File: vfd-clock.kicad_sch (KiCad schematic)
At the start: 93 parts, among them J1 ARGB, J2 ESP-Connector, J3 I2C, J4 SWD, J5 Power Input, Q1 FDS2734, SW1 PTS815, U1 IV-17, U10 LT3757AEMSE, U11 MIC4811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

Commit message: Final workings
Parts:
- C21: footprint Capacitor_SMD:C_0603_1608Metric_Pad1.08x0.95mm_HandSolder -> Capacitor_SMD:C_0805_2012Metric_Pad1.18x1.45mm_HandSolder
- C22: footprint Resistor_SMD:R_0603_1608Metric_Pad0.98x0.95mm_HandSolder -> Capacitor_SMD:C_0603_1608Metric_Pad1.08x0.95mm_HandSolder
- C23: footprint Capacitor_SMD:C_1206_3216Metric_Pad1.33x1.80mm_HandSolder -> Capacitor_SMD:C_0805_2012Metric_Pad1.18x1.45mm_HandSolder
- D2: footprint Diode_SMD:D_SMB_Handsoldering -> Diode_SMD:D_SMF
- U14: value ~ -> SN74HCS08
- U8: value ~ -> SN74HCS541
- U9: value ~ -> HV5812
- V1, V2: footprint mynixies:mynixies-IV-1 -> mynixies:IV-1
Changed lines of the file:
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@@
 			)
 		)
-		(property "Footprint" "Capacitor_SMD:C_1206_3216Metric_Pad1.33x1.80mm_HandSolder"
+		(property "Footprint" "Capacitor_SMD:C_0805_2012Metric_Pad1.18x1.45mm_HandSolder"
 			(at 257.5052 261.62 0)
 			(effects
@@
 			)
 		)
-		(property "Value" "~"
-			(at 175.26 182.88 0)
+		(property "Value" "HV5812"
+			(at 175.26 223.52 0)
 			(effects
 				(font
@@
 			)
 		)
-		(property "Description" ""
+		(property "Description" "Unpolarized capacitor"
 			(at 91.44 191.77 0)
 			(effects
@@
 			)
 		)
-		(property "Value" "~"
-			(at 345.44 184.15 0)
+		(property "Value" "SN74HCS08"
+			(at 345.44 204.47 0)
 			(effects
 				(font
@@
 			)
 		)
-		(property "Footprint" "mynixies:mynixies-IV-1"
+		(property "Footprint" "mynixies:IV-1"
 			(at 401.32 130.81 0)
 			(effects
@@
 			)
 		)
-		(property "Description" ""
+		(property "Description" "Unpolarized capacitor"
 			(at 45.72 203.2 0)
 			(effects
@@
 			)
 		)
-		(property "Description" ""
+		(property "Description" "Power symbol creates a global label with name \"GND\" , ground"
 			(at 35.56 311.15 0)
 			(effects
@@
 			)
 		)
-		(property "Description" ""
+		(property "Description" "Mounting Hole without connection"
 			(at 26.67 326.39 0)
 			(effects
@@
 			)
 		)
-		(property "Description" ""
+		(property "Description" "Mounting Hole without connection"
 			(at 77.47 326.39 0)
 			(effects
@@
 			)
 		)
-		(property "Description" ""
+		(property "Description" "Power symbol creates a global label with name \"+5V\""
 			(at 290.83 265.43 0)
 			(effects
@@
 			)
 		)
-		(property "Description" ""
+		(property "Description" "Power symbol creates a global label with name \"+5V\""
 			(at 35.56 290.83 0)
 			(effects
@@
 			)
 		)
-		(property "Description" ""
+		(property "Description" "Resistor"
 			(at 292.1 194.31 0)
 			(effects
@@
 			)
 		)
-		(property "Description" ""
+		(property "Description" "Mounting Hole without connection"
 			(at 34.29 326.39 0)
 			(effects
@@
 			)
 		)
-		(property "Description" ""
+		(property "Description" "Unpolarized capacitor"
 			(at 294.64 271.78 0)
 			(effects
@@
 			)
 		)
-		(property "Description" ""
+		(property "Description" "Mounting Hole without connection"
 			(at 69.85 326.39 0)
 			(effects
@@
 			)
 		)
-		(property "Description" ""
+		(property "Description" "Mounting Hole without connection"
 			(at 85.09 326.39 0)
 			(effects
@@
 			)
 		)
-		(property "Description" ""
+		(property "Description" "Power symbol creates a global label with name \"+5V\""
 			(at 295.91 187.96 0)
 			(effects
@@
 			)
 		)
-		(property "Description" ""
+		(property "Description" "Unpolarized capacitor"
 			(at 349.25 228.6 0)
 			(effects
@@
 			)
 		)
-		(property "Description" ""
+		(property "Description" "Special symbol for telling ERC where power comes from"
 			(at 300.99 265.43 0)
 			(effects
@@
 			)
 		)
-		(property "Description" ""
+		(property "Description" "Unpolarized capacitor"
 			(at 123.19 255.27 0)
 			(effects
@@
 			)
 		)
-		(property "Description" ""
+		(property "Description" "500mA Step-Down Converter with Sleep Mode, adjustable Output Voltage, 4.75-28V input voltage, WSON-10"
 			(at 321.31 231.14 0)
 			(effects
@@
 			)
 		)
-		(property "Footprint" "mynixies:mynixies-IV-1"
+		(property "Footprint" "mynixies:IV-1"
 			(at 387.35 130.81 0)
 			(effects
@@
 			)
 		)
-		(property "Description" ""
+		(property "Description" "Unpolarized capacitor"
 			(at 116.84 255.27 0)
 			(effects
@@
 			)
 		)
-		(property "Description" ""
+		(property "Description" "Unpolarized capacitor"
 			(at 91.44 33.02 0)
 			(effects
@@
 			)
 		)
-		(property "Description" ""
+		(property "Description" "Unpolarized capacitor"
 			(at 129.54 255.27 0)
 			(effects
@@
 			)
 		)
-		(property "Description" ""
+		(property "Description" "Unpolarized capacitor"
 			(at 293.37 228.6 0)
 			(effects
@@
 			)
 		)
-		(property "Description" ""
+		(property "Description" "Unpolarized capacitor"
 			(at 86.36 33.02 0)
 			(effects
@@
 			)
 		)
-		(property "Description" ""
+		(property "Description" "Mounting Hole without connection"
 			(at 19.05 326.39 0)
 			(effects
@@
 			)
 		)
-		(property "Description" ""
+		(property "Description" "Power symbol creates a global label with name \"+5V\""
 			(at 311.15 184.15 0)
 			(effects
@@
 			)
 		)
-		(property "Description" ""
+		(property "Description" "Unpolarized capacitor"
 			(at 104.14 255.27 0)
 			(effects
@@
 			)
 		)
-		(property "Description" ""
+		(property "Description" "Unpolarized capacitor"
 			(at 332.74 274.32 0)
 			(effects
@@
 			)
 		)
-		(property "Description" ""
+		(property "Description" "Unpolarized capacitor"
 			(at 91.44 186.69 0)
 			(effects
@@
 			)
 		)
-		(property "Description" ""
+		(property "Description" "Mounting Hole without connection"
 			(at 49.53 326.39 0)
 			(effects
@@
 			)
 		)
-		(property "Description" ""
+		(property "Description" "Mounting Hole without connection"
 			(at 57.15 326.39 0)
 			(effects
@@
 		(on_board yes)
 		(dnp no)
-		(fields_autoplaced yes)
 		(property "Reference" "U8"
 			(at 120.65 20.32 0)
@@
 			)
 		)
-		(property "Value" "~"
-			(at 120.65 22.86 0)
+		(property "Value" "SN74HCS541"
+			(at 120.65 49.53 0)
 			(effects
 				(font
@@
 			)
 		)
-		(property "Description" ""
+		(property "Description" "Inductor"
 			(at 336.55 223.52 0)
 			(effects
@@
 			)
 		)
-		(property "Description" ""
+		(property "Description" "Unpolarized capacitor"
 			(at 321.31 274.32 0)
 			(effects
@@
 			)
 		)
-		(property "Description" ""
+		(property "Description" "Resistor"
 			(at 344.17 228.6 0)
 			(effects
@@
 			)
 		)
-		(property "Description" ""
+		(property "Description" "Unpolarized capacitor"
 			(at 110.49 255.27 0)
 			(effects
@@
 			)
 		)
-		(property "Datasheet" "https://www.ckswitches.com/media/2728/pts815.pdf"
+		(property "Datasheet" "~"
 			(at 27.94 204.47 0)
 			(effects
@@
 			)
 		)
-		(property "Description" ""
+		(property "Description" "Push button switch, generic, two pins"
 			(at 33.02 204.47 0)
 			(effects
@@
 			)
 		)
-		(property "Datasheet" "https://www.taiwansemi.com/assets/datasheet/pdf.php?pn=HS1FFL"
+		(property "Datasheet" "~"
 			(at 242.57 252.73 0)
 			(effects
@@
 			)
 		)
-		(property "Description" ""
+		(property "Description" "Resistor"
 			(at 344.17 238.76 0)
 			(effects
@@
 			)
 		)
-		(property "Footprint" "Capacitor_SMD:C_0603_1608Metric_Pad1.08x0.95mm_HandSolder"
+		(property "Footprint" "Capacitor_SMD:C_0805_2012Metric_Pad1.18x1.45mm_HandSolder"
 			(at 224.4852 289.56 0)
 			(effects
@@
 			)
 		)
-		(property "Description" ""
+		(property "Description" "Mounting Hole without connection"
 			(at 41.91 326.39 0)
 			(effects
@@
 			)
 		)
-		(property "Footprint" "Diode_SMD:D_SMB_Handsoldering"
+		(property "Footprint" "Diode_SMD:D_SMF"
 			(at 260.35 257.81 0)
 			(effects
@@
 			)
 		)
-		(property "Datasheet" "https://www.littelfuse.com/~/media/electronics/datasheets/tvs_diodes/littelfuse_tvs_diode_tpsmb_datasheet.pdf.pdf"
+		(property "Datasheet" "https://www.vishay.com/doc?85881"
 			(at 265.43 256.54 0)
 			(effects
@@
 			)
 		)
-		(property "Description" ""
+		(property "Description" "200W unidirectional Transil Transient Voltage Suppressor, 58Vrwm, SMF"
 			(at 265.43 257.81 0)
 			(effects
@@
 			)
 		)
-		(property "Footprint" "Resistor_SMD:R_0603_1608Metric_Pad0.98x0.95mm_HandSolder"
+		(property "Footprint" "Capacitor_SMD:C_0603_1608Metric_Pad1.08x0.95mm_HandSolder"
 			(at 246.38 185.7248 0)
 			(effects
@@
 			)
 		)
-		(property "Description" ""
+		(property "Description" "Resistor"
 			(at 299.72 194.31 0)
 			(effects

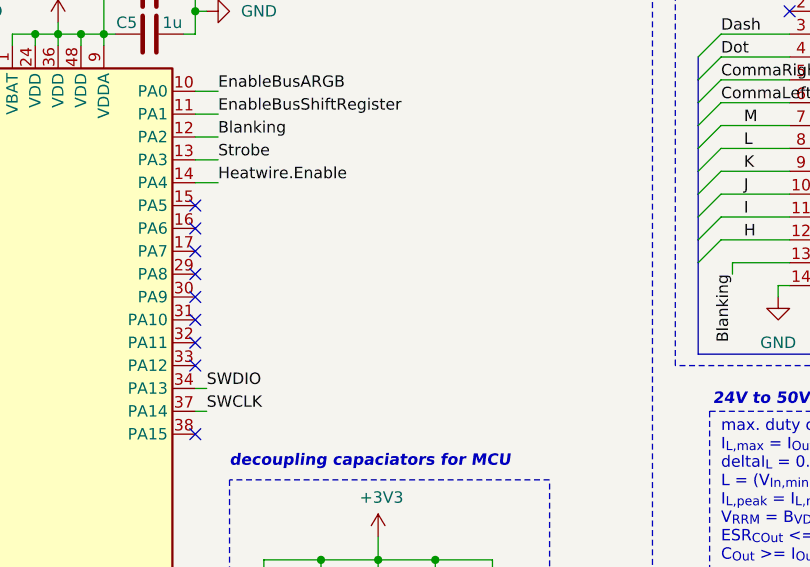
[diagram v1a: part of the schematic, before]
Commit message: Add ReadMe and a note to schematic
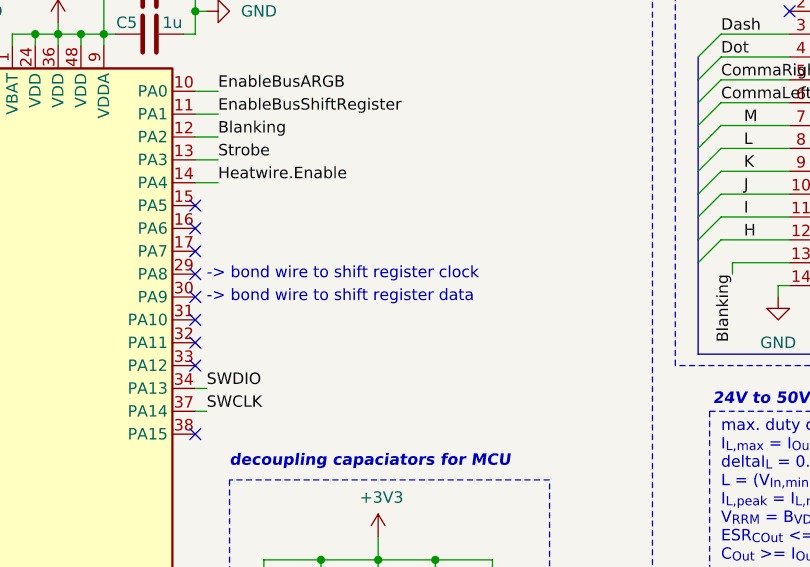
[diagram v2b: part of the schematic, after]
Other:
- note added: "-> bond wire to shift register clock"
- note added: "-> bond wire to shift register data"
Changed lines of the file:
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@@
+		)
+	)
+	(text "-> bond wire to shift register data"
+		(exclude_from_sim no)
+		(at 97.79 220.98 0)
+		(effects
+			(font
+				(size 1.27 1.27)
+			)
+			(justify left)
 		)
 	)
@@
 		(effects
 			(font
+				(size 1.27 1.27)
+			)
+			(justify left)
+		)
+	)
+	(text "-> bond wire to shift register clock"
+		(exclude_from_sim no)
+		(at 97.79 218.44 0)
+		(effects
+			(font
